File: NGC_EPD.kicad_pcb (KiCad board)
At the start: 2 copper layers, 79.9 x 34.9 mm, 54 parts, among them J1 Conn_ARM_JTAG_SWD_10, J2 EPD_FCC, Q1 NMOS, Q2 NMOS, U1 NGC1081, U2 TPS62125DSG

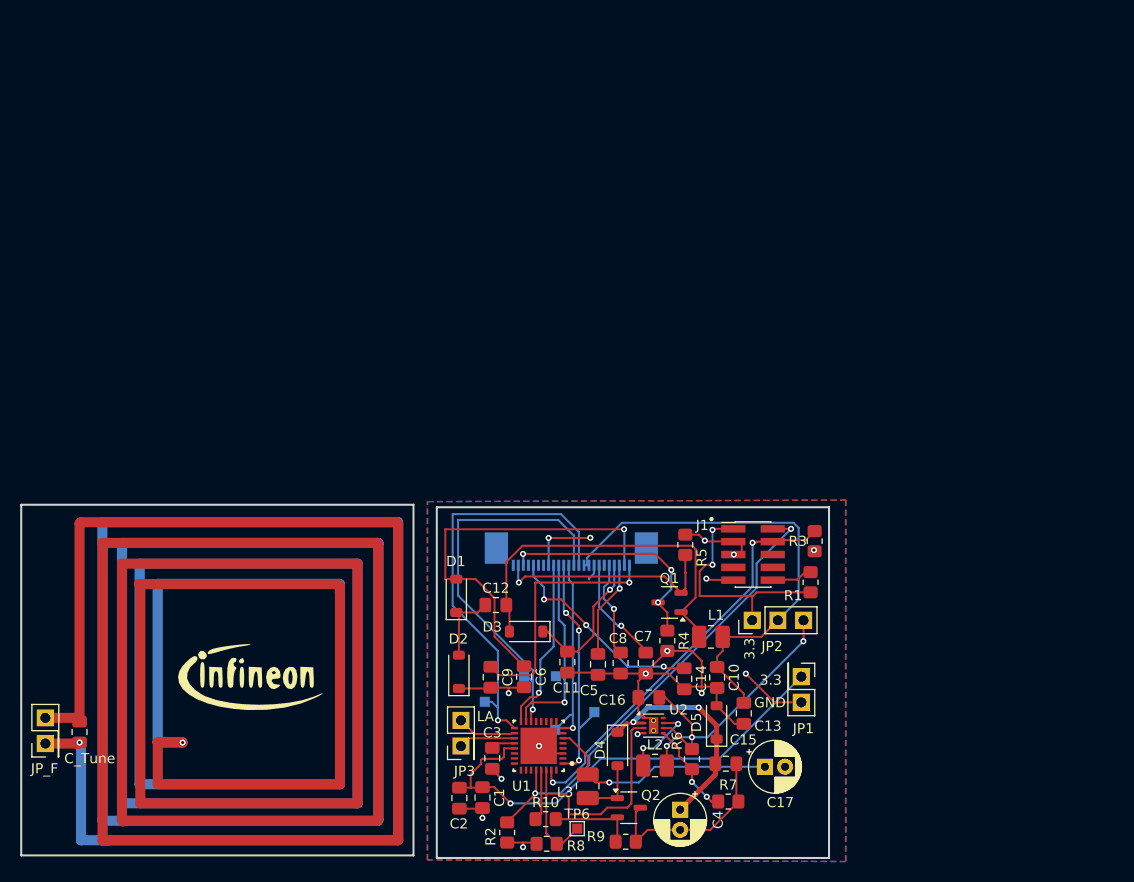
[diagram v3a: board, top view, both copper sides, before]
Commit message: Complete fresh layout. Grouped a functional block components. Placed all the required test points and changed sizes of components (mostly to 0603). Created a single board including antenna(snapable). Created a new antenna design(Draw lines->align->Convert them to tracks) which satisfies the net list.
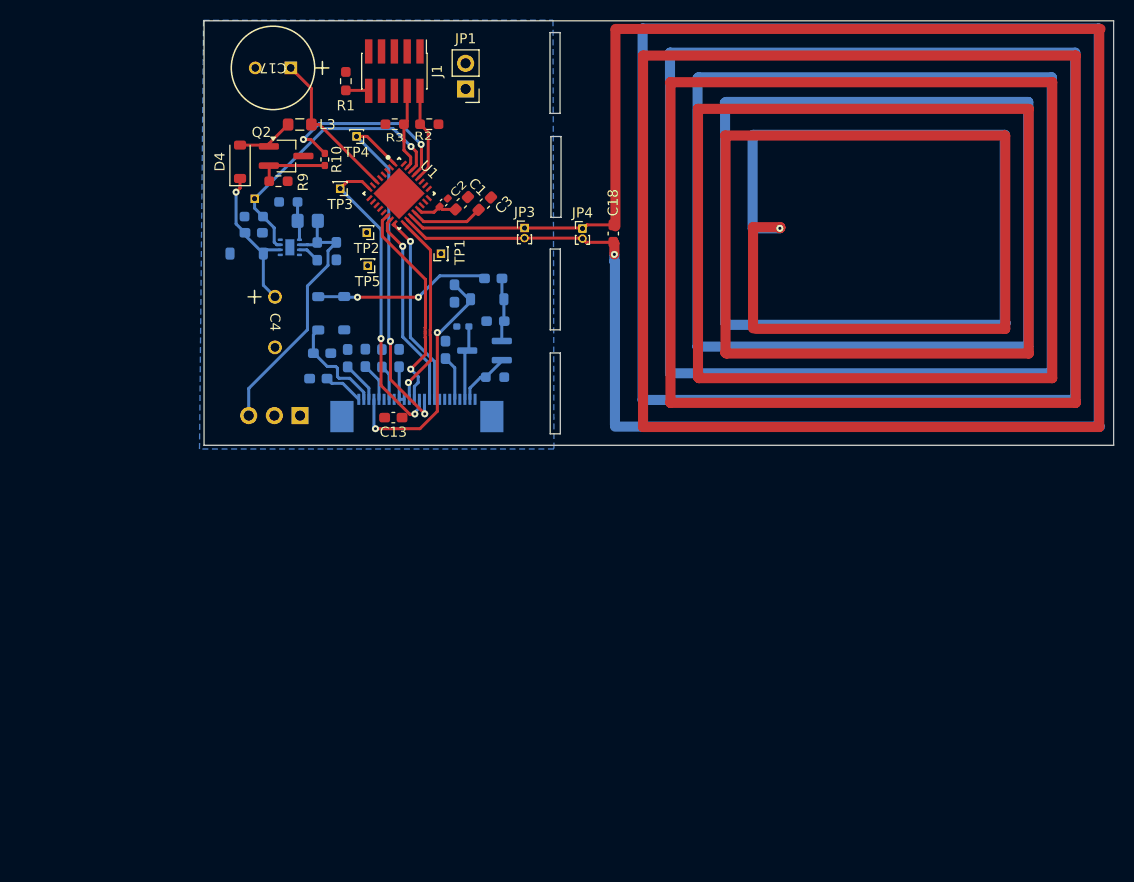
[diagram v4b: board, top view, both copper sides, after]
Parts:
- removed C_Tune: 4.7uF, Capacitor_SMD:C_0805_2012Metric_Pad1.18x1.45mm_HandSolder
- removed G*** (x2): LOGO, LOGO
- removed JP_F: ANT, Connector_PinHeader_2.54mm:PinHeader_2x01_P2.54mm_Vertical
- added C18: C_Tune, Capacitor_SMD:C_0603_1608Metric_Pad1.08x0.95mm_HandSolder, F.Cu at (143.1, 56.9)
- added JP4: EXT_SUP, Connector_PinHeader_1.00mm:PinHeader_1x02_P1.00mm_Vertical, F.Cu at (140.1, 56.4)
- C1, C13, C3: footprint Capacitor_SMD:C_0805_2012Metric_Pad1.18x1.45mm_HandSolder -> Capacitor_SMD:C_0603_1608Metric_Pad1.08x0.95mm_HandSolder
- C10, C11, C12, C14, C15, C16, C5, C6, C7, C8, C9: footprint Capacitor_SMD:C_0805_2012Metric_Pad1.18x1.45mm_HandSolder -> Capacitor_SMD:C_0603_1608Metric_Pad1.08x0.95mm_HandSolder; moved to B.Cu
- C17: footprint Capacitor_THT:CP_Radial_D5.0mm_P2.00mm -> NGC_EPD_FootprintLib:1mF_Nichicon UVR0J102MPD
- C2: footprint Capacitor_SMD:C_0805_2012Metric_Pad1.18x1.45mm_HandSolder -> Capacitor_SMD:C_0402_1005Metric_Pad0.74x0.62mm_HandSolder
- C4: value 5mF -> 4.7mF; footprint Capacitor_THT:CP_Radial_D5.0mm_P2.00mm -> NGC_EPD_FootprintLib:CAP_PK&slash_PZ_12P5X25_LOW_RUB
- D1, D2, D3, D5, JP2, R6: moved to B.Cu
- D4: value D_Schottky_Small -> D
- JP1: footprint Connector_PinHeader_2.54mm:PinHeader_2x01_P2.54mm_Vertical -> Connector_PinHeader_2.54mm:PinHeader_1x02_P2.54mm_Vertical
- JP3: value ANT -> EXT_SUP; footprint Connector_PinHeader_2.54mm:PinHeader_2x01_P2.54mm_Vertical -> Connector_PinHeader_1.00mm:PinHeader_1x02_P1.00mm_Vertical
- L1, L2: footprint Inductor_SMD:L_1008_2520Metric_Pad1.43x2.20mm_HandSolder -> Inductor_SMD:L_0603_1608Metric_Pad1.05x0.95mm_HandSolder; moved to B.Cu
- L3: footprint Inductor_SMD:L_1008_2520Metric_Pad1.43x2.20mm_HandSolder -> Inductor_SMD:L_0805_2012Metric_Pad1.05x1.20mm_HandSolder
- Q1: footprint Package_TO_SOT_SMD:SOT-23-3 -> Package_TO_SOT_SMD:TSOT-23_HandSoldering; moved to B.Cu
- Q2: footprint Package_TO_SOT_SMD:SOT-23-3 -> Package_TO_SOT_SMD:TSOT-23_HandSoldering
- R1, R2, R3, R9: footprint Resistor_SMD:R_0805_2012Metric_Pad1.20x1.40mm_HandSolder -> Resistor_SMD:R_0603_1608Metric_Pad0.98x0.95mm_HandSolder
- R10: footprint Resistor_SMD:R_0805_2012Metric_Pad1.20x1.40mm_HandSolder -> Resistor_SMD:R_0402_1005Metric_Pad0.72x0.64mm_HandSolder
- R4: footprint Resistor_SMD:R_0805_2012Metric_Pad1.20x1.40mm_HandSolder -> Resistor_SMD:R_0402_1005Metric_Pad0.72x0.64mm_HandSolder; moved to B.Cu
- R5, R7, R8: footprint Resistor_SMD:R_0805_2012Metric_Pad1.20x1.40mm_HandSolder -> Resistor_SMD:R_0603_1608Metric_Pad0.98x0.95mm_HandSolder; moved to B.Cu
- TP1, TP2, TP3, TP4, TP5: footprint TestPoint:TestPoint_Pad_1.0x1.0mm -> Connector_PinHeader_1.00mm:PinHeader_1x01_P1.00mm_Vertical; moved to F.Cu
- TP6: footprint TestPoint:TestPoint_Pad_1.0x1.0mm -> Connector_PinHeader_1.00mm:PinHeader_1x01_P1.00mm_Vertical; moved to B.Cu
- U2: footprint Package_SON:WSON-8-1EP_2x2mm_P0.5mm_EP0.9x1.6mm_ThermalVias -> Package_SON:WSON-8-1EP_2x2mm_P0.5mm_EP0.9x1.6mm; moved to B.Cu
- moved C17 83.6 mm to (111.2, 40.5), turned to 180 degrees
- moved R9 73.8 mm to (110.0, 51.8)
- moved R7 73.6 mm to (111.0, 53.8), turned to 180 degrees
- moved Q2 72.9 mm to (110.8, 49.3)
- moved L3 71.4 mm to (112.1, 46.1), turned to 180 degrees
- moved R2 70.5 mm to (124.9, 46.1), turned to 0 degrees
- moved C15 70.3 mm to (107.6, 56.9)
- moved TP6 70.0 mm to (107.7, 53.5), turned to 180 degrees
- moved D4 69.1 mm to (106.2, 49.8), turned to 90 degrees
- moved R10 68.8 mm to (114.6, 49.6), turned to -90 degrees
- moved R8 68.5 mm to (107.6, 55.3)
- moved R1 67.6 mm to (116.7, 41.9), turned to -90 degrees
- moved JP1 67.0 mm to (128.5, 42.6), turned to 180 degrees
- moved D5 65.7 mm to (106.9, 58.9), turned to 180 degrees
- moved R6 65.4 mm to (112.9, 55.7), turned to 180 degrees
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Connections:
- JP3 pad 2: Net-(JP3-B) -> Net-(JP3-A)
- U1 pad 18: Net-(JP3-B) -> Net-(JP3-A)
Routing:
- net Net-(JP3-A): track 5.61 -> 1358.4 mm, vias 0 -> 2
- net (no net): track 811.7 -> 0.00 mm, vias 2 -> 0
- net GND: track 101.9 -> 0.00 mm, vias 16 -> 0
- net +3.3V: track 70.2 -> 4.20 mm, vias 3 -> 0
- net EPD3p3: track 48.2 -> 3.73 mm
- net SWDIO: track 46.3 -> 9.39 mm, vias 2 -> 0
- net SWDCLK: track 39.8 -> 8.15 mm, vias 2 -> 0
- net Net-(D3-A): track 36.8 -> 6.39 mm
- net PREVGL: track 39.8 -> 10.3 mm, vias 1 -> 0
- net SDA: track 42.3 -> 19.5 mm
- net VCOM: track 24.7 -> 3.99 mm, vias 1 -> 0
- net SCL: track 39.2 -> 21.2 mm
- net GDR: track 22.7 -> 5.47 mm, vias 1 -> 0
- net VSH2: track 20.5 -> 4.42 mm, vias 3 -> 0
- net RESE: track 23.3 -> 7.37 mm, vias 3 -> 0
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- removed copper zone on F.Cu, net +3.3V
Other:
- board size 79.9 x 34.9 mm -> 90 x 42 mm
- board text removed: "3.3"
- board text removed: "GND"
- board text removed: "LA"

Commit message: Routing complete.Added logo.DRC zero errors. Readjusted antenna routing. Added dimensions in user comments layer.
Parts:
- added G***: LOGO, LOGO, F.Cu at (170.5, 56.5)
- added G***: LOGO, LOGO, F.Cu at (110.2, 57.5)
- moved TP5 5.14 mm to (123.9, 59.2)
- moved C13 1.58 mm to (119.8, 75.2)
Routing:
- net +3.3V: track 4.20 -> 82.9 mm
- net EPD3p3: track 3.73 -> 36.0 mm, vias 0 -> 3
- net GND: track 0.00 -> 27.6 mm, vias 0 -> 14
- net RES#: track 19.7 -> 21.7 mm
- net SCL: track 21.2 -> 22.8 mm
- net SDA: track 19.5 -> 20.7 mm
- net Net-(JP3-A): track 1358.4 -> 1357.8 mm
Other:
- board text added: "3.3V"
- board text added: "BUCK"
- board text added: "EPD_Sup"
- board text added: "GND"
